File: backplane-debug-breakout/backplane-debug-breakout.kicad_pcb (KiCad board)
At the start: 2 copper layers, 65 x 50.5 mm, 11 parts, among them J1 Conn_02x08_Odd_Even, J2 Conn_01x04, J3 Conn_01x01_Socket, J4 Conn_01x01_Socket, J5 Conn_01x04, SW2 SW_Omron_B3FS, SW3 EG1218, U1 UMFT234XF

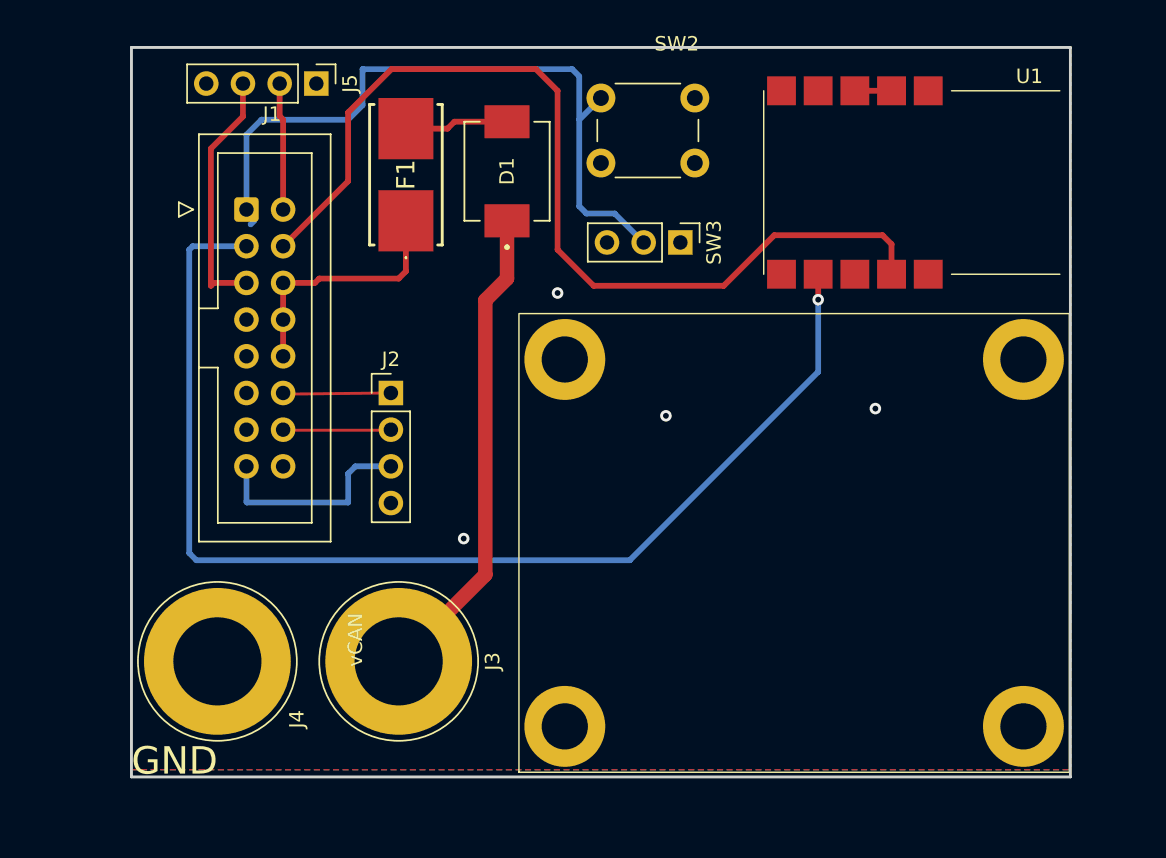
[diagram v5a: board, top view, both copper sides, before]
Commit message: added vias, adjusted labels
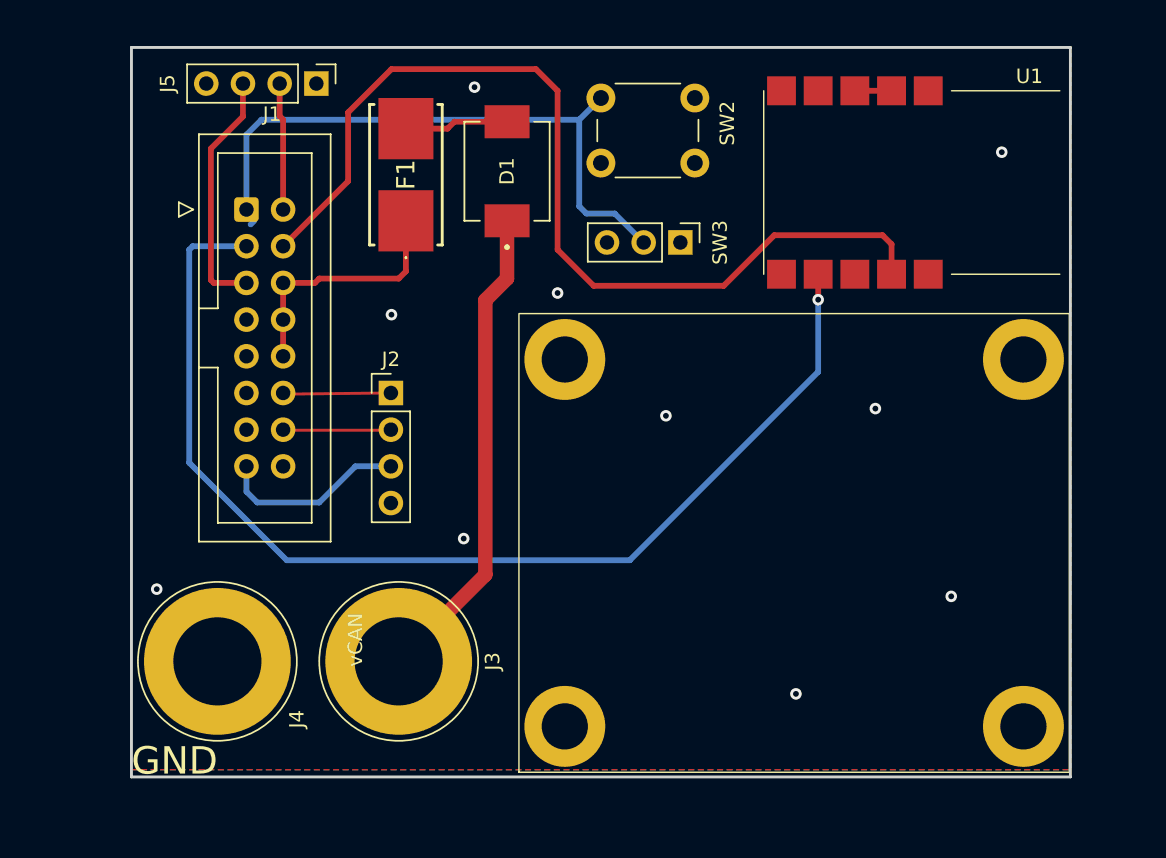
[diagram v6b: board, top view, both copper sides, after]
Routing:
- net /SD: track 48.7 -> 42.6 mm
- net /C3-UART-TX: track 81.0 -> 77.4 mm
- net /OPD_SCL: track 14.7 -> 13.1 mm
- net GND: vias 4 -> 10
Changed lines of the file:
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@@
 		(tags "tact sw push 6mm")
 		(property "Reference" "SW2"
-			(at 1.25 8.25 180)
+			(at -2.25 2.75 -90)
 			(layer "F.SilkS")
 			(effects
@@
 		(tags "Through hole pin header THT 1x03 2.54mm single row")
 		(property "Reference" "SW3"
-			(at 0 -2.33 90)
+			(at 0 -2.75 90)
 			(layer "F.SilkS")
 			(effects
@@
 		(at 123 67.57 90)
 		(property "Reference" "D1"
-			(at 0 0 270)
+			(at 0 0 -90)
 			(layer "F.SilkS")
 			(effects
@@
 		)
 		(property "Value" "TSM MURS315SH"
-			(at 0 -1 270)
+			(at 0 -1 -90)
 			(layer "F.Fab")
 			(effects
@@
 		(tags "Through hole pin header THT 1x04 2.54mm single row")
 		(property "Reference" "J5"
-			(at 0 -2.33 90)
+			(at 0 10.3 90)
 			(layer "F.SilkS")
 			(effects
@@
 		(tags "Fuse")
 		(property "Reference" "F1"
-			(at 0 0 270)
+			(at 0 0 -90)
 			(layer "F.SilkS")
 			(effects
@@
 		)
 		(property "Value" "Fuseholder"
-			(at -11.5 -5.5 270)
+			(at -11.5 -5.5 -90)
 			(layer "F.SilkS")
 			(hide yes)
@@
 		)
 		(fp_text user "${REFERENCE}"
-			(at 0 -4.5 270)
+			(at 0 -4.5 -90)
 			(layer "F.Fab")
 			(effects
@@
 	)
 	(segment
-		(start 104.72 63.78)
-		(end 102.5 66)
+		(start 102.5 66)
+		(end 102.5 75.1)
 		(width 0.4)
 		(layer "F.Cu")
@@
 	)
 	(segment
-		(start 102.5 66)
-		(end 102.5 75.5)
+		(start 104.72 63.78)
+		(end 102.5 66)
 		(width 0.4)
 		(layer "F.Cu")
@@
 	)
 	(segment
-		(start 102.7 75.3)
-		(end 104.96 75.3)
+		(start 104.72 61.5)
+		(end 104.72 63.78)
 		(width 0.4)
 		(layer "F.Cu")
@@
 	)
 	(segment
-		(start 102.5 75.5)
-		(end 102.7 75.3)
+		(start 102.7 75.3)
+		(end 104.96 75.3)
 		(width 0.4)
 		(layer "F.Cu")
@@
 	)
 	(segment
-		(start 104.72 61.5)
-		(end 104.72 63.78)
+		(start 102.5 75.1)
+		(end 102.7 75.3)
 		(width 0.4)
 		(layer "F.Cu")
@@
 	)
 	(segment
-		(start 101 94)
-		(end 101.5 94.5)
+		(start 131.5 94.5)
+		(end 144.54 81.46)
 		(width 0.4)
 		(layer "B.Cu")
@@
 	)
 	(segment
-		(start 101.24 72.76)
-		(end 101 73)
+		(start 104.96 72.76)
+		(end 101.24 72.76)
 		(width 0.4)
 		(layer "B.Cu")
@@
 	)
 	(segment
-		(start 144.54 81.46)
-		(end 144.54 76.46)
+		(start 101.24 72.76)
+		(end 101 73)
 		(width 0.4)
 		(layer "B.Cu")
@@
 	)
 	(segment
-		(start 101.5 94.5)
-		(end 131.5 94.5)
+		(start 144.54 81.46)
+		(end 144.54 76.46)
 		(width 0.4)
 		(layer "B.Cu")
@@
 	)
 	(segment
-		(start 104.96 72.76)
-		(end 101.24 72.76)
+		(start 101 73)
+		(end 101 87.75)
 		(width 0.4)
 		(layer "B.Cu")
@@
 	)
 	(segment
-		(start 101 73)
-		(end 101 94)
+		(start 107.75 94.5)
+		(end 131.5 94.5)
 		(width 0.4)
 		(layer "B.Cu")
@@
 	)
 	(segment
-		(start 131.5 94.5)
-		(end 144.54 81.46)
+		(start 101 87.75)
+		(end 107.75 94.5)
 		(width 0.4)
 		(layer "B.Cu")
@@
 	)
 	(via
+		(at 153.75 97)
+		(size 0.8)
+		(drill 0.4)
+		(layers "F.Cu" "B.Cu")
+		(free yes)
+		(net 6)
+	)
+	(via
 		(at 120 93)
 		(size 0.8)
@@
 	)
 	(via
+		(at 120.75 61.75)
+		(size 0.8)
+		(drill 0.4)
+		(layers "F.Cu" "B.Cu")
+		(free yes)
+		(net 6)
+	)
+	(via
+		(at 115 77.5)
+		(size 0.8)
+		(drill 0.4)
+		(layers "F.Cu" "B.Cu")
+		(free yes)
+		(net 6)
+	)
+	(via
 		(at 134 84.5)
 		(size 0.8)
@@
 		(net 6)
 	)
+	(via
+		(at 143 103.75)
+		(size 0.8)
+		(drill 0.4)
+		(layers "F.Cu" "B.Cu")
+		(free yes)
+		(net 6)
+	)
+	(via
+		(at 98.75 96.5)
+		(size 0.8)
+		(drill 0.4)
+		(layers "F.Cu" "B.Cu")
+		(free yes)
+		(net 6)
+	)
+	(via
+		(at 157.25 66.25)
+		(size 0.8)
+		(drill 0.4)
+		(layers "F.Cu" "B.Cu")
+		(free yes)
+		(net 6)
+	)
 	(segment
 		(start 149.62 74.7)
@@
 	)
 	(segment
-		(start 114.96 88)
-		(end 112.5 88)
-		(width 0.4)
-		(layer "B.Cu")
-		(net 9)
-	)
-	(segment
 		(start 112.5 88)
-		(end 112 88.5)
+		(end 110 90.5)
 		(width 0.4)
 		(layer "B.Cu")
@@
 	)
 	(segment
-		(start 105 90.5)
-		(end 104.96 90.46)
+		(start 105.71 90.5)
+		(end 104.96 89.75)
 		(width 0.4)
 		(layer "B.Cu")
@@
 	)
 	(segment
-		(start 104.96 90.46)
-		(end 104.96 88)
+		(start 114.96 88)
+		(end 112.5 88)
 		(width 0.4)
 		(layer "B.Cu")
@@
 	)
 	(segment
-		(start 112 88.5)
-		(end 112 90.5)
+		(start 110 90.5)
+		(end 105.71 90.5)
 		(width 0.4)
 		(layer "B.Cu")
@@
 	)
 	(segment
-		(start 112 90.5)
-		(end 105 90.5)
+		(start 104.96 89.75)
+		(end 104.96 88)
 		(width 0.4)
 		(layer "B.Cu")
@@
 	)
 	(segment
-		(start 104.96 65.04)
-		(end 106 64)
+		(start 106 64)
+		(end 128 64)
 		(width 0.4)
 		(layer "B.Cu")
@@
 	)
 	(segment
-		(start 127.5 60.5)
-		(end 128 61)
+		(start 104.96 65.04)
+		(end 106 64)
 		(width 0.4)
 		(layer "B.Cu")
@@
 	)
 	(segment
-		(start 113 60.5)
-		(end 127.5 60.5)
+		(start 104.96 70.22)
+		(end 104.96 65.04)
 		(width 0.4)
 		(layer "B.Cu")
@@
 	)
 	(segment
-		(start 128 61)
-		(end 128 64)
-		(width 0.4)
-		(layer "B.Cu")
-		(net 11)
-	)
-	(segment
-		(start 112 64)
-		(end 113 63)
-		(width 0.4)
-		(layer "B.Cu")
-		(net 11)
-	)
-	(segment
-		(start 113 63)
-		(end 113 60.5)
-		(width 0.4)
-		(layer "B.Cu")
-		(net 11)
-	)
-	(segment
-		(start 104.96 70.22)
-		(end 104.96 65.04)
-		(width 0.4)
-		(layer "B.Cu")
-		(net 11)
-	)
-	(segment
 		(start 130.46 70.5)
 		(end 132.46 72.5)
 		(width 0.4)
 		(layer "B.Cu")
-		(net 11)
-	)
-	(segment
-		(start 106 64)
-		(end 112 64)
-		(width 0.4)
-		(layer "B.Cu")

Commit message: Random clean, including some value changes, and moving the vulcan connector around to minimize wire lengths.
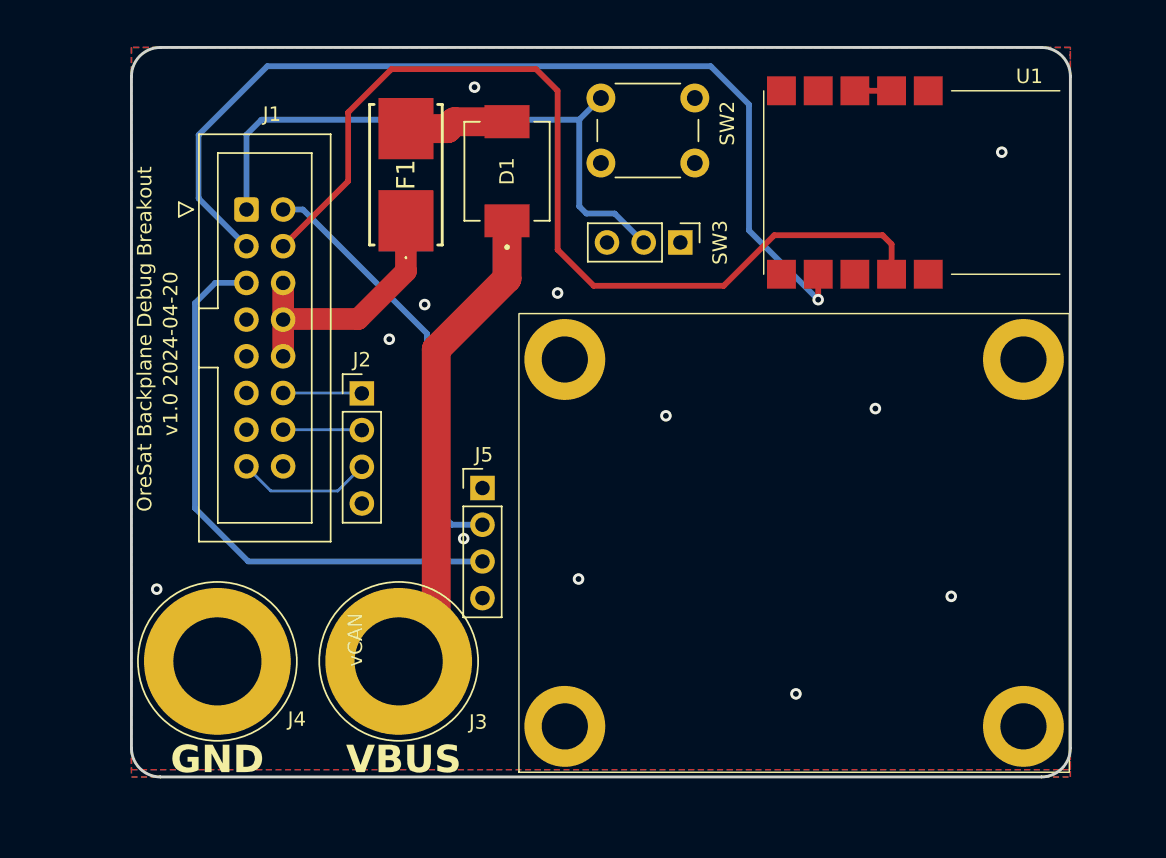
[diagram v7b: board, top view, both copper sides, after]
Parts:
- F1: value Fuseholder -> 01550900DR
- moved J5 30.3 mm to (121.3, 89.5), turned to 0 degrees
- moved J2 2.01 mm to (113.0, 83.0)
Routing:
- net /CAN_H: track 17.1 -> 39.8 mm
- net /CAN_L: track 8.82 -> 29.6 mm
- net /C3-UART-TX: track 77.4 -> 67.5 mm
- net /OPD_SDA: track 0.00 -> 5.46 mm
- net /OPD_PWR: track 0.00 -> 5.46 mm
- net /OPD_SCL: track 13.1 -> 9.87 mm
- net /VBUS: track 17.4 -> 18.5 mm
- net GND: vias 10 -> 12
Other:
- outline, holes or cut-outs redrawn
- board text added: "${TITLE}"
- board text added: "VBUS"
- board text added: "v${REVISION} ${ISSUE_DATE}"
